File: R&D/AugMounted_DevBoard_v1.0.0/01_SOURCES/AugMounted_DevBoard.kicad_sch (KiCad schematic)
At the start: 0 parts

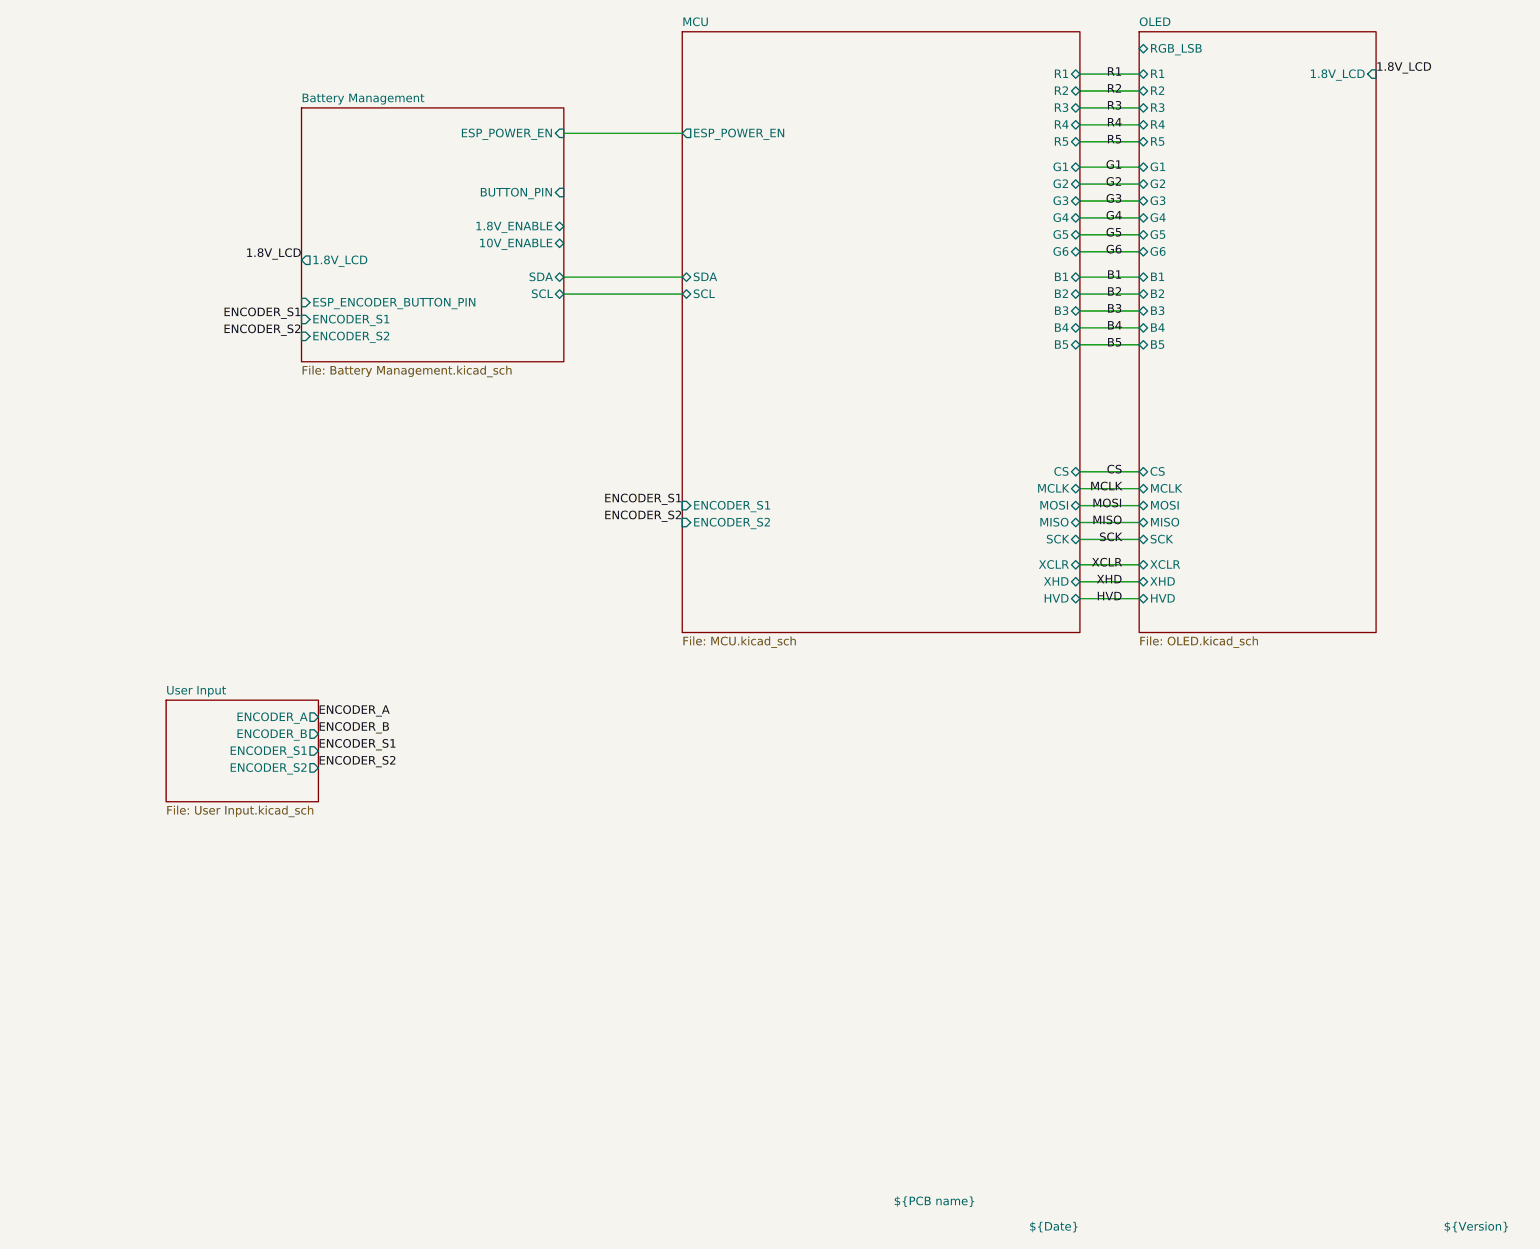
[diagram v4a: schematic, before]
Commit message: Schematic done
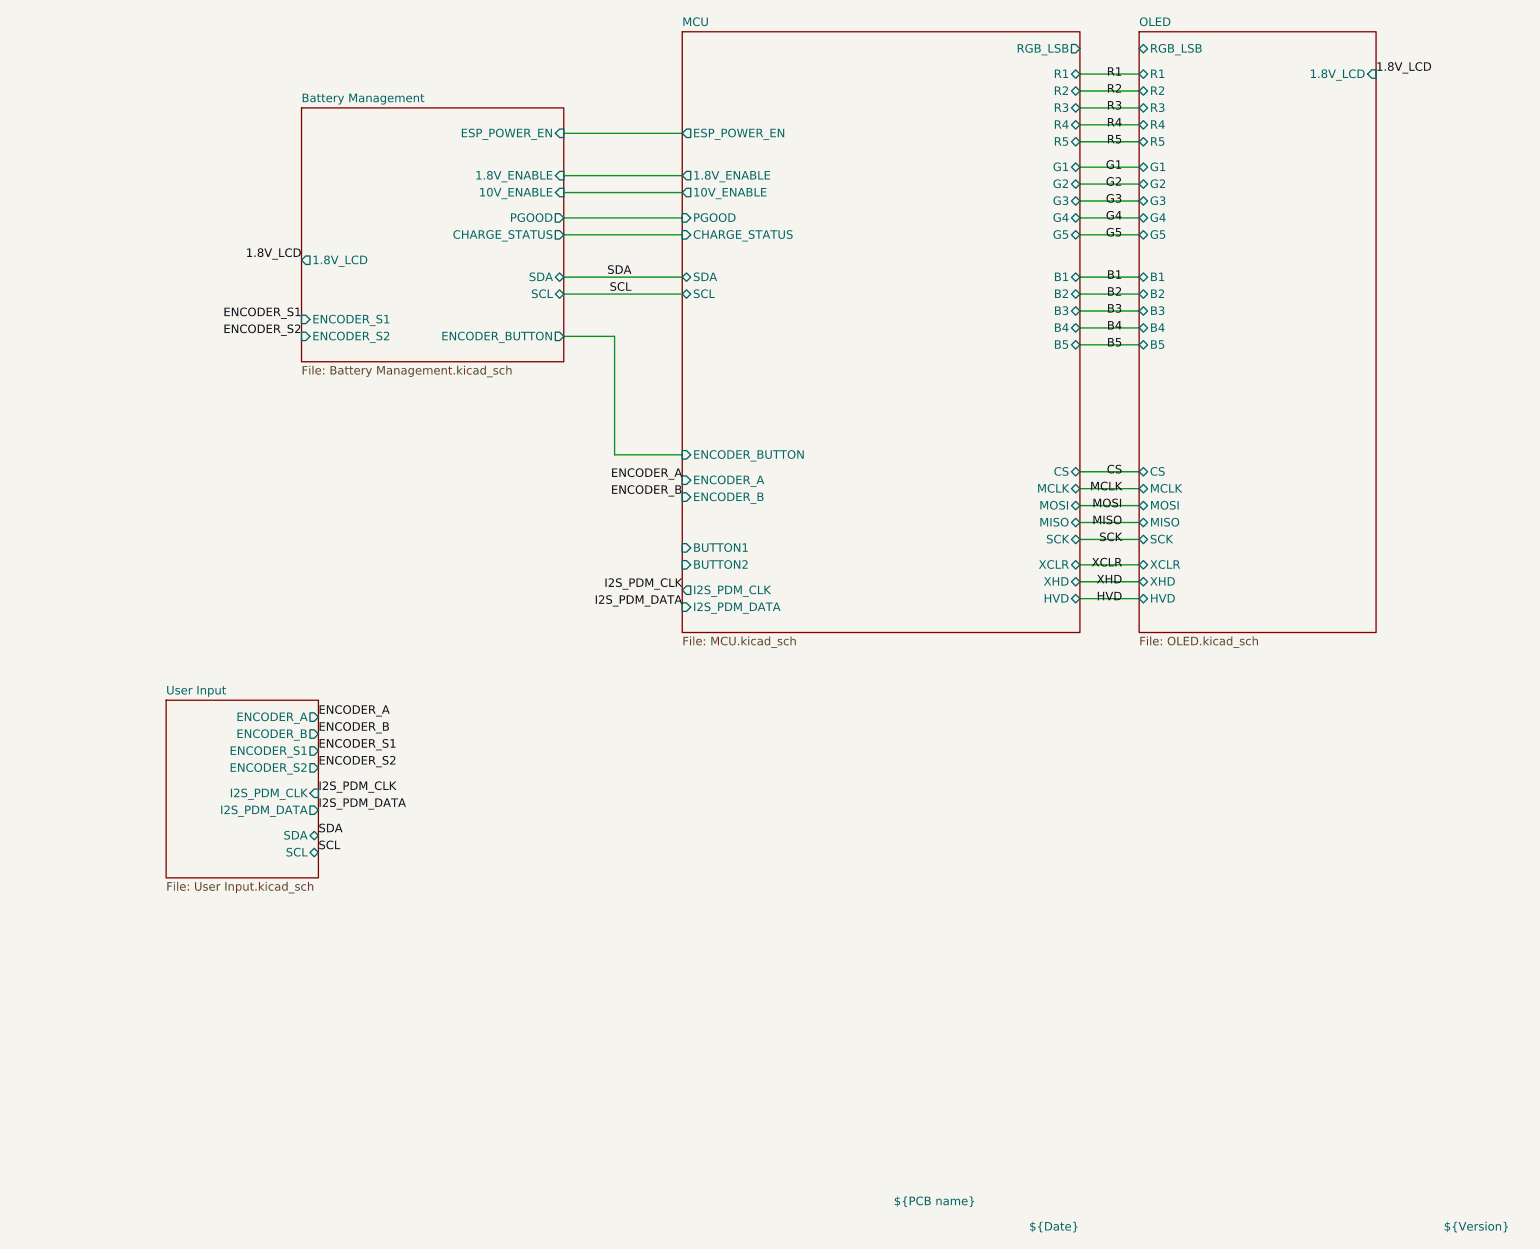
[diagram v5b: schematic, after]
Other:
- sheet Battery Management ports: added CHARGE_STATUS, ENCODER_BUTTON, PGOOD; removed BUTTON_PIN, ESP_ENCODER_BUTTON_PIN
- sheet MCU ports: added 1.8V_ENABLE, 10V_ENABLE, BUTTON1, BUTTON2, CHARGE_STATUS, ENCODER_A, ENCODER_B, ENCODER_BUTTON, I2S_PDM_CLK, I2S_PDM_DATA, PGOOD, RGB_LSB; removed ENCODER_S1, ENCODER_S2, G6
- sheet OLED ports: added none; removed G6
- sheet User Input ports: added I2S_PDM_CLK, I2S_PDM_DATA, SCL, SDA; removed none
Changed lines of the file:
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@@
+    (stroke (width 0) (type default))
+  )
+  (wire (pts (xy 144.78 77.47) (xy 154.94 77.47))
     (stroke (width 0) (type default))
   )
@@
     (stroke (width 0) (type default))
   )
+  (wire (pts (xy 137.16 59.69) (xy 144.78 59.69))
+    (stroke (width 0) (type default))
+  )
   (wire (pts (xy 214.63 20.32) (xy 223.52 20.32))
     (stroke (width 0) (type default))
@@
     (stroke (width 0) (type default))
   )
+  (wire (pts (xy 137.16 35.56) (xy 154.94 35.56))
+    (stroke (width 0) (type default))
+  )
   (wire (pts (xy 214.63 34.29) (xy 223.52 34.29))
     (stroke (width 0) (type default))
@@
     (stroke (width 0) (type default))
   )
-  (wire (pts (xy 214.63 46.99) (xy 223.52 46.99))
+  (wire (pts (xy 137.16 44.45) (xy 154.94 44.45))
+    (stroke (width 0) (type default))
+  )
+  (wire (pts (xy 137.16 41.91) (xy 154.94 41.91))
     (stroke (width 0) (type default))
   )
@@
     (stroke (width 0) (type default))
   )
+  (wire (pts (xy 144.78 59.69) (xy 144.78 77.47))
+    (stroke (width 0) (type default))
+  )
   (wire (pts (xy 214.63 93.98) (xy 223.52 93.98))
     (stroke (width 0) (type default))
   )
+  (wire (pts (xy 137.16 38.1) (xy 154.94 38.1))
+    (stroke (width 0) (type default))
+  )
   (wire (pts (xy 214.63 41.91) (xy 223.52 41.91))
     (stroke (width 0) (type default))
@@
     (effects (font (size 1.27 1.27)) (justify right bottom))
   )
+  (label "I2S_PDM_CLK" (at 154.94 97.79 180) (fields_autoplaced)
+    (effects (font (size 1.27 1.27)) (justify right bottom))
+  )
   (label "B5" (at 220.98 60.96 180) (fields_autoplaced)
     (effects (font (size 1.27 1.27)) (justify right))
@@
     (effects (font (size 1.27 1.27)) (justify right))
   )
+  (label "I2S_PDM_CLK" (at 100.33 128.27 0) (fields_autoplaced)
+    (effects (font (size 1.27 1.27)) (justify left bottom))
+  )
   (label "R3" (at 220.98 25.4 180) (fields_autoplaced)
     (effects (font (size 1.27 1.27)) (justify right))
@@
     (effects (font (size 1.27 1.27)) (justify right))
   )
-  (label "G6" (at 220.98 46.99 180) (fields_autoplaced)
-    (effects (font (size 1.27 1.27)) (justify right))
+  (label "I2S_PDM_DATA" (at 154.94 100.33 180) (fields_autoplaced)
+    (effects (font (size 1.27 1.27)) (justify right bottom))
   )
   (label "ENCODER_S1" (at 100.33 121.92 0) (fields_autoplaced)
@@
     (effects (font (size 1.27 1.27)) (justify right bottom))
   )
-  (label "ENCODER_S1" (at 154.94 85.09 180) (fields_autoplaced)
-    (effects (font (size 1.27 1.27)) (justify right bottom))
+  (label "I2S_PDM_DATA" (at 100.33 130.81 0) (fields_autoplaced)
+    (effects (font (size 1.27 1.27)) (justify left bottom))
   )
   (label "XHD" (at 220.98 96.52 180) (fields_autoplaced)
     (effects (font (size 1.27 1.27)) (justify right))
   )
+  (label "SCL" (at 147.32 53.34 180) (fields_autoplaced)
+    (effects (font (size 1.27 1.27)) (justify right bottom))
+  )
   (label "ENCODER_A" (at 100.33 116.84 0) (fields_autoplaced)
     (effects (font (size 1.27 1.27)) (justify left bottom))
@@
     (effects (font (size 1.27 1.27)) (justify right))
   )
+  (label "ENCODER_B" (at 154.94 83.82 180) (fields_autoplaced)
+    (effects (font (size 1.27 1.27)) (justify right bottom))
+  )
   (label "CS" (at 220.98 80.01 180) (fields_autoplaced)
     (effects (font (size 1.27 1.27)) (justify right))
@@
     (effects (font (size 1.27 1.27)) (justify right))
   )
+  (label "SDA" (at 100.33 134.62 0) (fields_autoplaced)
+    (effects (font (size 1.27 1.27)) (justify left bottom))
+  )
   (label "MOSI" (at 220.98 85.09 180) (fields_autoplaced)
     (effects (font (size 1.27 1.27)) (justify right))
   )
+  (label "SCL" (at 100.33 137.16 0) (fields_autoplaced)
+    (effects (font (size 1.27 1.27)) (justify left bottom))
+  )
+  (label "SDA" (at 147.32 50.8 180) (fields_autoplaced)
+    (effects (font (size 1.27 1.27)) (justify right bottom))
+  )
   (label "MISO" (at 220.98 87.63 180) (fields_autoplaced)
     (effects (font (size 1.27 1.27)) (justify right))
   )
-  (label "ENCODER_S2" (at 154.94 87.63 180) (fields_autoplaced)
+  (label "ENCODER_A" (at 154.94 81.28 180) (fields_autoplaced)
     (effects (font (size 1.27 1.27)) (justify right bottom))
   )
@@
     (effects (font (size 1.27 1.27)) (justify left bottom))
   )
-  (sheet (at 77.47 114.3) (size 22.86 15.24) (fields_autoplaced)
+  (sheet (at 77.47 114.3) (size 22.86 26.67) (fields_autoplaced)
     (stroke (width 0.1524) (type solid))
     (fill (color 0 0 0 0.0000))
@@
       (effects (font (size 1.27 1.27)) (justify left bottom))
     )
-    (property "Sheetfile" "User Input.kicad_sch" (at 77.47 130.1246 0)
+    (property "Sheetfile" "User Input.kicad_sch" (at 77.47 141.5546 0)
       (effects (font (size 1.27 1.27)) (justify left top))
     )
@@
     )
     (pin "ENCODER_S1" output (at 100.33 121.92 0)
+      (effects (font (size 1.27 1.27)) (justify right))
+    )
+    (pin "I2S_PDM_CLK" input (at 100.33 128.27 0)
+      (effects (font (size 1.27 1.27)) (justify right))
+    )
+    (pin "I2S_PDM_DATA" output (at 100.33 130.81 0)
+      (effects (font (size 1.27 1.27)) (justify right))
+    )
+    (pin "SDA" bidirectional (at 100.33 134.62 0)
+      (effects (font (size 1.27 1.27)) (justify right))
+    )
+    (pin "SCL" bidirectional (at 100.33 137.16 0)
       (effects (font (size 1.27 1.27)) (justify right))
     )
@@
       (effects (font (size 1.27 1.27)) (justify right))
     )
-    (pin "BUTTON_PIN" input (at 137.16 38.1 0)
-      (effects (font (size 1.27 1.27)) (justify right))
-    )
     (pin "ESP_POWER_EN" input (at 137.16 29.21 0)
       (effects (font (size 1.27 1.27)) (justify right))
     )
-    (pin "1.8V_ENABLE" bidirectional (at 137.16 43.18 0)
-      (effects (font (size 1.27 1.27)) (justify right))
-    )
-    (pin "10V_ENABLE" bidirectional (at 137.16 45.72 0)
+    (pin "ENCODER_S1" input (at 97.79 57.15 180)
+      (effects (font (size 1.27 1.27)) (justify left))
+    )
+    (pin "ENCODER_S2" input (at 97.79 59.69 180)
+      (effects (font (size 1.27 1.27)) (justify left))
+    )
+    (pin "1.8V_ENABLE" input (at 137.16 35.56 0)
       (effects (font (size 1.27 1.27)) (justify right))
     )
@@
       (effects (font (size 1.27 1.27)) (justify left))
     )
-    (pin "ENCODER_S1" input (at 97.79 57.15 180)
-      (effects (font (size 1.27 1.27)) (justify left))
-    )
-    (pin "ENCODER_S2" input (at 97.79 59.69 180)
-      (effects (font (size 1.27 1.27)) (justify left))
-    )
-    (pin "ESP_ENCODER_BUTTON_PIN" input (at 97.79 54.61 180)
-      (effects (font (size 1.27 1.27)) (justify left))
+    (pin "ENCODER_BUTTON" output (at 137.16 59.69 0)
+      (effects (font (size 1.27 1.27)) (justify right))
+    )
+    (pin "10V_ENABLE" input (at 137.16 38.1 0)
+      (effects (font (size 1.27 1.27)) (justify right))
+    )
+    (pin "PGOOD" output (at 137.16 41.91 0)
+      (effects (font (size 1.27 1.27)) (justify right))
+    )
+    (pin "CHARGE_STATUS" output (at 137.16 44.45 0)
+      (effects (font (size 1.27 1.27)) (justify right))
     )
     (instances
@@
       (effects (font (size 1.27 1.27)) (justify left))
     )
-    (pin "G6" bidirectional (at 223.52 46.99 180)
-      (effects (font (size 1.27 1.27)) (justify left))
-    )
     (pin "B2" bidirectional (at 223.52 53.34 180)
       (effects (font (size 1.27 1.27)) (justify left))
@@
       (effects (font (size 1.27 1.27)) (justify right))
     )
-    (pin "G6" bidirectional (at 214.63 46.99 0)
-      (effects (font (size 1.27 1.27)) (justify right))
-    )
     (pin "HVD" bidirectional (at 214.63 99.06 0)
       (effects (font (size 1.27 1.27)) (justify right))
@@
       (effects (font (size 1.27 1.27)) (justify left))
     )
-    (pin "ENCODER_S1" input (at 154.94 85.09 180)
-      (effects (font (size 1.27 1.27)) (justify left))
-    )
-    (pin "ENCODER_S2" input (at 154.94 87.63 180)
-      (effects (font (size 1.27 1.27)) (justify left))
-    )
+    (pin "I2S_PDM_CLK" output (at 154.94 97.79 180)
+      (effects (font (size 1.27 1.27)) (justify left))
+    )
+    (pin "I2S_PDM_DATA" input (at 154.94 100.33 180)
+      (effects (font (size 1.27 1.27)) (justify left))
+    )
+    (pin "BUTTON1" input (at 154.94 91.44 180)
+      (effects (font (size 1.27 1.27)) (justify left))
+    )
+    (pin "RGB_LSB" output (at 214.63 16.51 0)
+      (effects (font (size 1.27 1.27)) (justify right))
+    )
+    (pin "10V_ENABLE" output (at 154.94 38.1 180)
+      (effects (font (size 1.27 1.27)) (justify left))
+    )
+    (pin "ENCODER_BUTTON" input (at 154.94 77.47 180)
+      (effects (font (size 1.27 1.27)) (justify left))
+    )
+    (pin "BUTTON2" input (at 154.94 93.98 180)
+      (effects (font (size 1.27 1.27)) (justify left))
+    )
+    (pin "1.8V_ENABLE" output (at 154.94 35.56 180)
+      (effects (font (size 1.27 1.27)) (justify left))
+    )
+    (pin "ENCODER_A" input (at 154.94 81.28 180)
+      (effects (font (size 1.27 1.27)) (justify left))
+    )
+    (pin "ENCODER_B" input (at 154.94 83.82 180)
+      (effects (font (size 1.27 1.27)) (justify left))
+    )
+    (pin "PGOOD" input (at 154.94 41.91 180)
+      (effects (font (size 1.27 1.27)) (justify left))
+    )
+    (pin "CHARGE_STATUS" input (at 154.94 44.45 180)
+      (effects (font (size 1.27 1.27)) (justify left))
+    )

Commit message: First revision of the layout
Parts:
- added LOGO1: mounted_logo, .mounted-lib:mounted_logo, symbol .mounted-lib:mounted_logo
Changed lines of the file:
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@@
     (effects (font (size 1.27 1.27)) (justify left bottom))
+  )
+  (symbol (lib_id ".mounted-lib:mounted_logo") (at 227.33 173.99 0) (unit 1)
+    (in_bom yes) (on_board yes) (dnp no) (fields_autoplaced)
+    (property "Reference" "LOGO1" (at 227.33 167.64 0)
+      (effects (font (size 1.27 1.27)) hide)
+    )
+    (property "Value" "mounted_logo" (at 267.97 173.99 0)
+      (effects (font (size 1.27 1.27)) hide)
+    )
+    (property "Footprint" ".mounted-lib:mounted_logo" (at 273.05 171.45 0)
+      (effects (font (size 1.27 1.27)) hide)
+    )
+    (property "Datasheet" "" (at 227.33 173.99 0)
+      (effects (font (size 1.27 1.27)) hide)
+    )
+    (instances
+      (project "AugMounted_DevBoard"
+        (path "/75b08848-9393-425e-a17d-60105119a7b1"
+          (reference "LOGO1") (unit 1)
+        )
+      )
+    )
   )
   (sheet (at 77.47 114.3) (size 22.86 26.67) (fields_autoplaced)
